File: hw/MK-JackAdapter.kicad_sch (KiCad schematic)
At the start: 2 parts, among them J2 KEY-PADDLE-8, J7 KEY-PADDLE-4

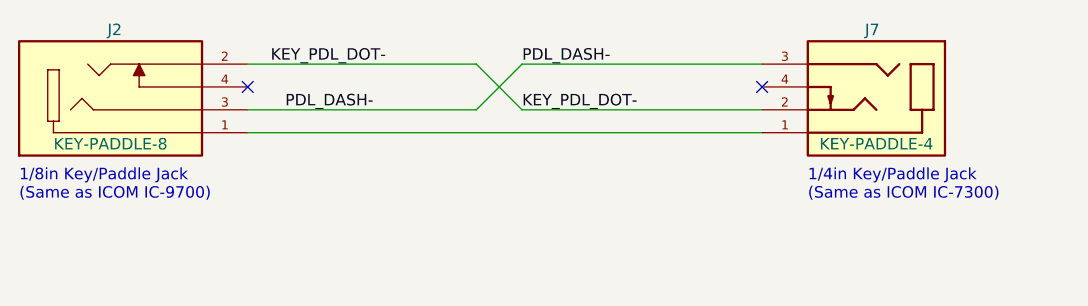
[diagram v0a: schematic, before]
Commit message: KSInf-MkIII: New  JA: Add terminal block
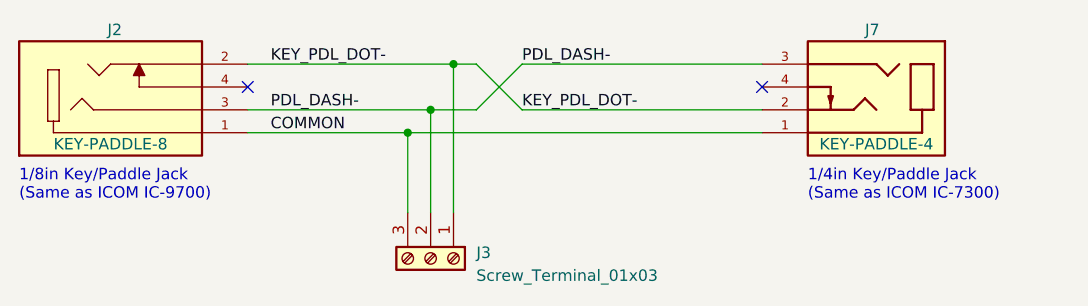
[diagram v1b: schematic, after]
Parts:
- added J3: Screw_Terminal_01x03, TerminalBlock_Philmore:TerminalBlock_Philmore_TB133_1x03_P5.00mm_Horizontal, symbol Connector:Screw_Terminal_01x03
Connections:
- net KEY_PDL_DOT-: now also J3.1 (Pin_1)
- net PDL_DASH-: now also J3.2 (Pin_2)
- net COMMON: now reaches J2.1, J7.1
- net COMMON: now also J3.3 (Pin_3)
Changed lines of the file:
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@@
     (comment 1 "Copyright 2023-24 AESilky")
+  )
+  (junction (at 128.27 97.79) (diameter 0) (color 0 0 0 0)
+  )
+  (junction (at 130.81 92.71) (diameter 0) (color 0 0 0 0)
+  )
+  (junction (at 125.73 100.33) (diameter 0) (color 0 0 0 0)
   )
   (no_connect (at 165.1 95.25))
   (no_connect (at 107.95 95.25))
-  (wire (pts (xy 107.95 100.33) (xy 165.1 100.33))
+  (wire (pts (xy 128.27 97.79) (xy 133.35 97.79))
+    (stroke (width 0) (type default))
+  )
+  (wire (pts (xy 107.95 100.33) (xy 125.73 100.33))
+    (stroke (width 0) (type default))
+  )
+  (wire (pts (xy 125.73 100.33) (xy 165.1 100.33))
+    (stroke (width 0) (type default))
+  )
+  (wire (pts (xy 130.81 92.71) (xy 130.81 109.22))
     (stroke (width 0) (type default))
   )
@@
     (stroke (width 0) (type default))
   )
+  (wire (pts (xy 125.73 100.33) (xy 125.73 109.22))
+    (stroke (width 0) (type default))
+  )
   (wire (pts (xy 133.35 97.79) (xy 138.43 92.71))
     (stroke (width 0) (type default))
   )
-  (wire (pts (xy 133.35 92.71) (xy 107.95 92.71))
+  (wire (pts (xy 133.35 92.71) (xy 130.81 92.71))
     (stroke (width 0) (type default))
   )
-  (wire (pts (xy 107.95 97.79) (xy 133.35 97.79))
+  (wire (pts (xy 128.27 97.79) (xy 128.27 109.22))
     (stroke (width 0) (type default))
   )
   (wire (pts (xy 133.35 92.71) (xy 138.43 97.79))
+    (stroke (width 0) (type default))
+  )
+  (wire (pts (xy 107.95 97.79) (xy 128.27 97.79))
+    (stroke (width 0) (type default))
+  )
+  (wire (pts (xy 130.81 92.71) (xy 107.95 92.71))
     (stroke (width 0) (type default))
   )
@@
     (effects (font (size 1.27 1.27)) (justify left bottom))
   )
-  (label "PDL_DASH-" (at 121.92 97.79 180) (fields_autoplaced)
-    (effects (font (size 1.27 1.27)) (justify right bottom))
+  (label "PDL_DASH-" (at 110.49 97.79 0) (fields_autoplaced)
+    (effects (font (size 1.27 1.27)) (justify left bottom))
   )
   (label "PDL_DASH-" (at 138.43 92.71 0) (fields_autoplaced)
+    (effects (font (size 1.27 1.27)) (justify left bottom))
+  )
+  (label "COMMON" (at 110.49 100.33 0) (fields_autoplaced)
     (effects (font (size 1.27 1.27)) (justify left bottom))
   )
@@
         )
       )
-      (project "MK_JackAdapter"
+      (project "MK-JackAdapter"
         (path "/6e8b5822-411f-4ce7-8db2-57346eba4281"
           (reference "J1") (unit 1)
@@
     (pin "4")
     (instances
-      (project "MK_JackAdapter"
+      (project "MK-JackAdapter"
         (path "/6e8b5822-411f-4ce7-8db2-57346eba4281"
           (reference "J2") (unit 1)
@@
         )
       )
+    )
+  )
+  (symbol (lib_id "Connector:Screw_Terminal_01x03") (at 128.27 114.3 270) (unit 1)
+    (in_bom yes) (on_board yes) (dnp no) (fields_autoplaced)
+    (property "Reference" "J3" (at 133.35 113.665 90)
+      (effects (font (size 1.27 1.27)) (justify left))
+    )
+    (property "Value" "Screw_Terminal_01x03" (at 133.35 116.205 90)
+      (effects (font (size 1.27 1.27)) (justify left))
+    )
+    (property "Footprint" "TerminalBlock_Philmore:TerminalBlock_Philmore_TB133_1x03_P5.00mm_Horizontal" (at 128.27 114.3 0)
+      (effects (font (size 1.27 1.27)) hide)
+    )
+    (property "Datasheet" "~" (at 128.27 114.3 0)
+      (effects (font (size 1.27 1.27)) hide)
+    )
+    (pin "1")
+    (pin "2")
+    (pin "3")
+    (instances
+      (project "MK-JackAdapter"
+        (path "/6e8b5822-411f-4ce7-8db2-57346eba4281"
+          (reference "J3") (unit 1)
+        )
+      )
